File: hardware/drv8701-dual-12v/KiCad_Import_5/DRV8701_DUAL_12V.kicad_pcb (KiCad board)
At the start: 4 copper layers, 48 x 36 mm, 38 parts, among them CN1 XT30UPB-M, CN2 XT30UPB-M, CN3 XH2.54-4P, P2 XT30UPB-M, Q1 TPH1R403NL, Q2 TPH1R403NL, Q3 TPH1R403NL, Q4 TPH1R403NL, Q5 TPH1R403NL, Q6 TPH1R403NL, Q7 TPH1R403NL, Q8 TPH1R403NL, U1 DRV8701ERGET, U2 DRV8701ERGET, U5 SS12D10G4

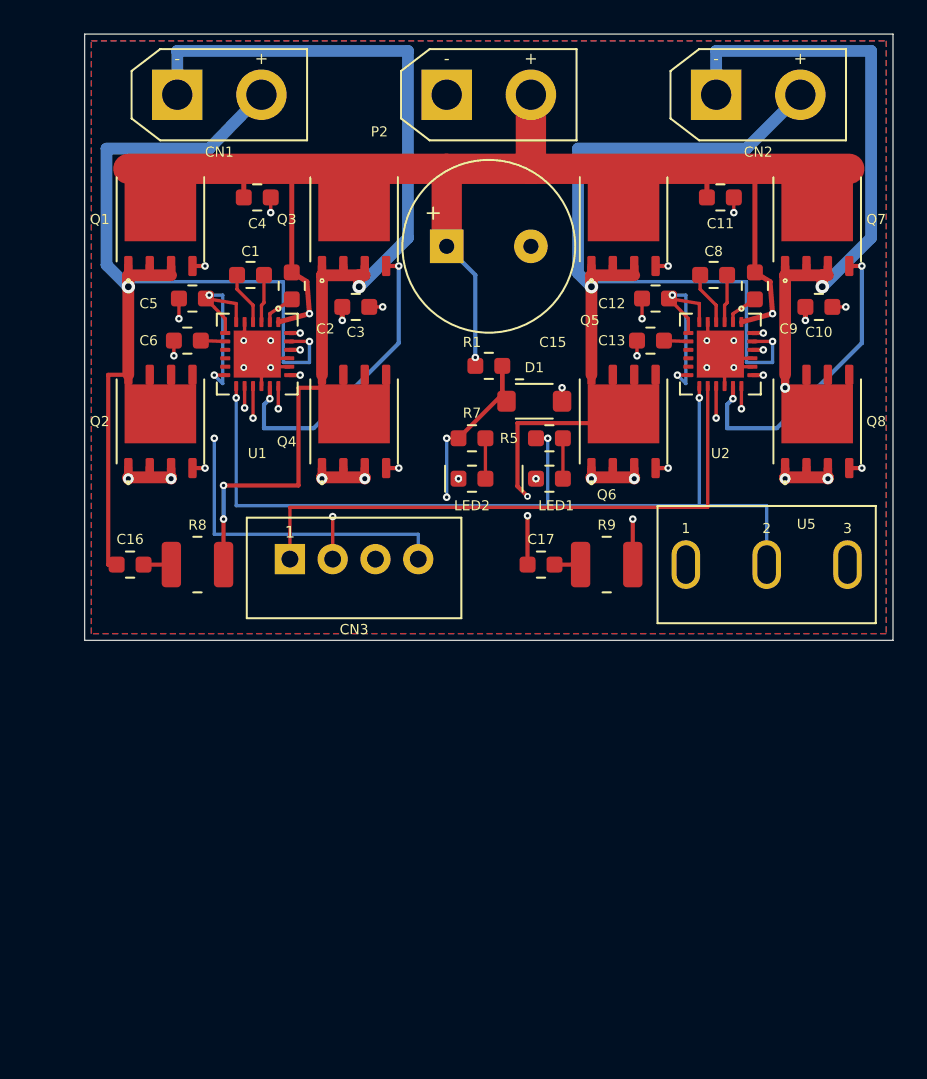
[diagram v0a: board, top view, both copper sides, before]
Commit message: Rework DRV8701 Rev B power control and manual PCB layout
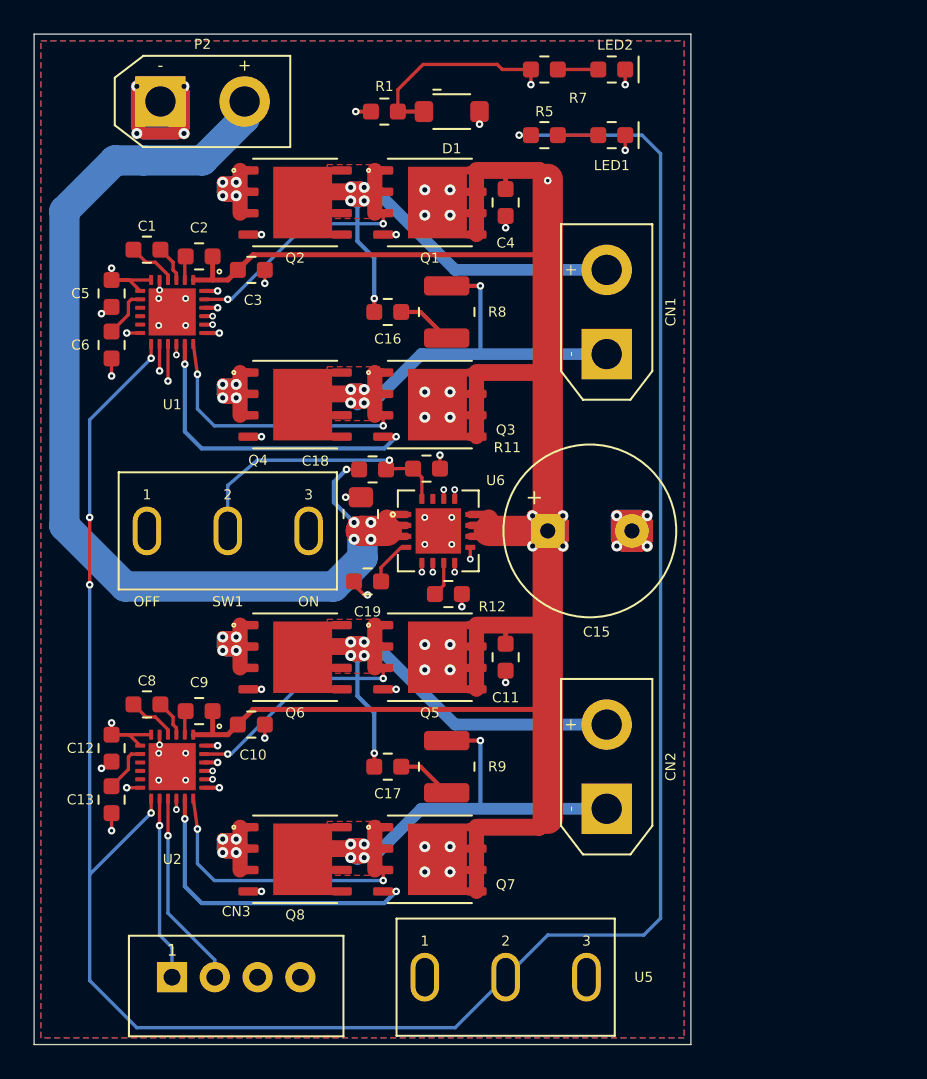
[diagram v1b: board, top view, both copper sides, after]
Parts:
- added C18: 4.7uF, DRV8701_Custom:C_0805_2012Metric, F.Cu at (16.4, 28.5)
- added C19: 10nF, DRV8701_Custom:C_0603_1608Metric, F.Cu at (16.8, 32.5)
- added R10: 100kΩ, DRV8701_Custom:R_0603_1608Metric, F.Cu at (17.1, 25.9)
- added R11: 33kΩ, DRV8701_Custom:R_0603_1608Metric, F.Cu at (20.3, 25.8)
- added R12: 40.2kΩ, DRV8701_Custom:R_0603_1608Metric, F.Cu at (21.6, 33.2)
- added SW1: SS12D10G4, DRV8701_Custom:SS12D10G4, F.Cu at (8.50, 29.5)
- added U6: TPS25910RSAR, DRV8701_Custom:TPS25910_RSA16, F.Cu at (21.0, 29.5)
- moved Q7 44.4 mm to (20.5, 49.0), turned to 270 degrees
- moved C8 42.2 mm to (3.70, 39.8)
- moved C13 42.0 mm to (1.60, 45.5), turned to 270 degrees
- moved C12 41.9 mm to (1.60, 42.4), turned to 270 degrees
- moved C10 41.8 mm to (9.90, 41.0)
- moved C9 41.6 mm to (6.80, 40.2), turned to 0 degrees
- moved CN2 40.9 mm to (31.0, 43.5), turned to 90 degrees
- moved U2 40.7 mm to (5.20, 43.5)
- moved Q8 40.5 mm to (12.5, 49.0), turned to 270 degrees
- moved C11 30.1 mm to (25.0, 37.0), turned to 270 degrees
- moved U5 29.0 mm to (25.0, 56.0)
- moved Q5 28.4 mm to (20.5, 37.0), turned to 270 degrees
- moved CN1 26.4 mm to (31.0, 16.5), turned to 90 degrees
- moved CN3 25.8 mm to (9.00, 56.0)
- moved LED2 25.7 mm to (31.3, 2.10), turned to 180 degrees
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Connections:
- P2 pad 1: VM -> VM_RAW
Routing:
- net VM: track 127.8 -> 255.6 mm, vias 5 -> 22
- net GND: track 30.8 -> 118.2 mm, vias 27 -> 65
- net NSLEEP: track 53.9 -> 138.0 mm, vias 3 -> 5
- net VM_RAW: track 0.00 -> 75.6 mm, vias 0 -> 5
- net 3V3: track 39.5 -> 78.5 mm, vias 2 -> 1
- net L_EN_IN: track 23.1 -> 56.1 mm, vias 2 -> 1
- net L_PH_IN: track 17.5 -> 47.0 mm
- net R_EN_IN: track 35.1 -> 10.9 mm, vias 0 -> 1
- net R_PH_IN: track 33.0 -> 11.8 mm, vias 2 -> 1
- net L_B: track 82.0 -> 63.5 mm, vias 4 -> 7
- net R_B: track 80.7 -> 63.5 mm, vias 4 -> 7
- net PWR_EN: track 0.00 -> 17.1 mm, vias 0 -> 1
- net R_A: track 76.6 -> 62.3 mm, vias 4 -> 7
- net L_A: track 70.6 -> 62.3 mm, vias 2 -> 7
- net L_GL2: track 14.8 -> 7.49 mm
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- added copper zone on F.Cu, net L_A
- added copper zone on F.Cu, net L_B
- added copper zone on F.Cu, net R_A
- added copper zone on F.Cu, net R_B
- added copper zone on In2.Cu, net VM
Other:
- board size 48 x 36 mm -> 39 x 60 mm
- board text added: "12V / 1.8A x2"
- board text added: "C18"
- board text added: "C19"
- board text added: "DRV8701 DUAL / REV B"
- board text added: "MAIN POWER"
- board text added: "OFF"
- board text added: "ON"
- board text added: "R10"
- board text added: "R11"
- board text added: "R12"
- board text added: "SLEEP ENABLE"
- board text added: "SW1"
- board text added: "U6"
- board text removed: "DRV8701 DUAL / 12V"
- board text removed: "SOURCE VALUES / REV A"
